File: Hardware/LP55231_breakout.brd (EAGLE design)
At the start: 25.4 x 25.4 mm, 13 parts

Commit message: PCB Work in progress.
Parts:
- removed LED3: LED-TRICOLOR-NO-COMPLCC-6-SMD, SparkFun-LED:PLCC-6-LED
- added FD1, FD2: FIDUCIALUFIDUCIAL, SparkFun-Aesthetics:MICRO-FIDUCIAL
- added J1, J2, J3: (no value), SparkFun-Connectors:1X04_NO_SILK_ALL_ROUND
- added J4: (no value), SparkFun-Connectors:1X09_NO_SILK
- added JP3: I2C-PULLUPS, SparkFun-Passives:PAD-JUMPER-3-NC_BY_PASTE_YES_SILK_FULL_BOX
- added LED4: LED-TRICOLOR-5050NO_IC, SparkFun-LED:LED-TRICOLOR-5050
- added R1, R2: 4.7K, SparkFun-Resistors:0603-RES
- moved C2 11.1 mm to (8.89, 14.6), turned to 270 degrees
- moved LED2 8.98 mm to (19.1, 15.2), turned to 180 degrees
- moved LOGO1 8.03 mm to (17.8, 20.3)
- moved C1 8.03 mm to (14.0, 19.1)
- moved C3 6.75 mm to (10.2, 18.4), turned to 0 degrees
- moved LED1 5.24 mm to (19.1, 25.4), turned to 180 degrees
- moved JP1 5.08 mm to (11.4, 26.7)
- moved LOGO2 5.08 mm to (2.54, 1.27)
- moved JP2 5.08 mm to (10.2, 24.1)
- moved U$1 3.59 mm to (12.7, 15.2)
- moved C4 2.62 mm to (7.62, 17.1), turned to 90 degrees
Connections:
- net N$16 renamed ADDR1
- net N$17 renamed ADDR0
- removed net N$1: LED3.AR, U$1.11
- removed net N$10: C1.1, U$1.22
- removed net N$2: LED3.AG, U$1.15
- removed net N$3: LED3.AB, U$1.14
- removed net N$4: LED2.AB, U$1.16
- removed net N$5: LED2.AR, U$1.12
- removed net N$6: LED2.AG, U$1.17
- removed net N$7: LED1.AR, U$1.13
- removed net N$8: LED1.AG, U$1.19
- removed net N$9: LED1.AB, U$1.18
- new net B1: J1.4, LED1.AB, U$1.18
- new net B2: J2.4, LED2.AB, U$1.16
- new net B3: J3.4, LED4.3, U$1.14
- new net G1: J1.3, LED1.AG, U$1.19
- new net G2: J2.3, LED2.AG, U$1.17
- new net G3: J3.3, LED4.1, U$1.15
- new net N$15: U$1.7
- new net N$18: U$1.10
- new net N$19: U$1.5
- new net N$20: U$1.6
- new net N$21: JP3.1, R2.2
- new net N$22: JP3.3, R1.2
- new net R1: J1.1, LED1.AR, U$1.13
- new net R2: J2.1, LED2.AR, U$1.12
- new net R3: J3.1, LED4.2, U$1.11
- new net SCL: J4.4, R1.1, U$1.9
- new net SDA: J4.3, R2.1, U$1.8
- new net VOUT: C1.1, J4.9, U$1.22
- net GND: now also J1.2, J2.2, J3.2, J4.1, LED4.4, LED4.5, LED4.6; no longer LED3.CB, LED3.CG, LED3.CR
- net VCC: now also J4.2, JP3.2
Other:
- board size 25.4 x 25.4 mm -> 26.7 x 30.5 mm
- board text added: "B1"
- board text added: "B2"
- board text added: "B3"
- board text added: "G1"
- board text added: "G2"
- board text added: "G3"
- board text added: "GND"
- board text added: "R1"
- board text added: "R2"
- board text added: "R3"
- board text added: "SCL"
- board text added: "SDA"
- board text added: "V01"
- board text added: "VCC"
- board text added: "VOUT"

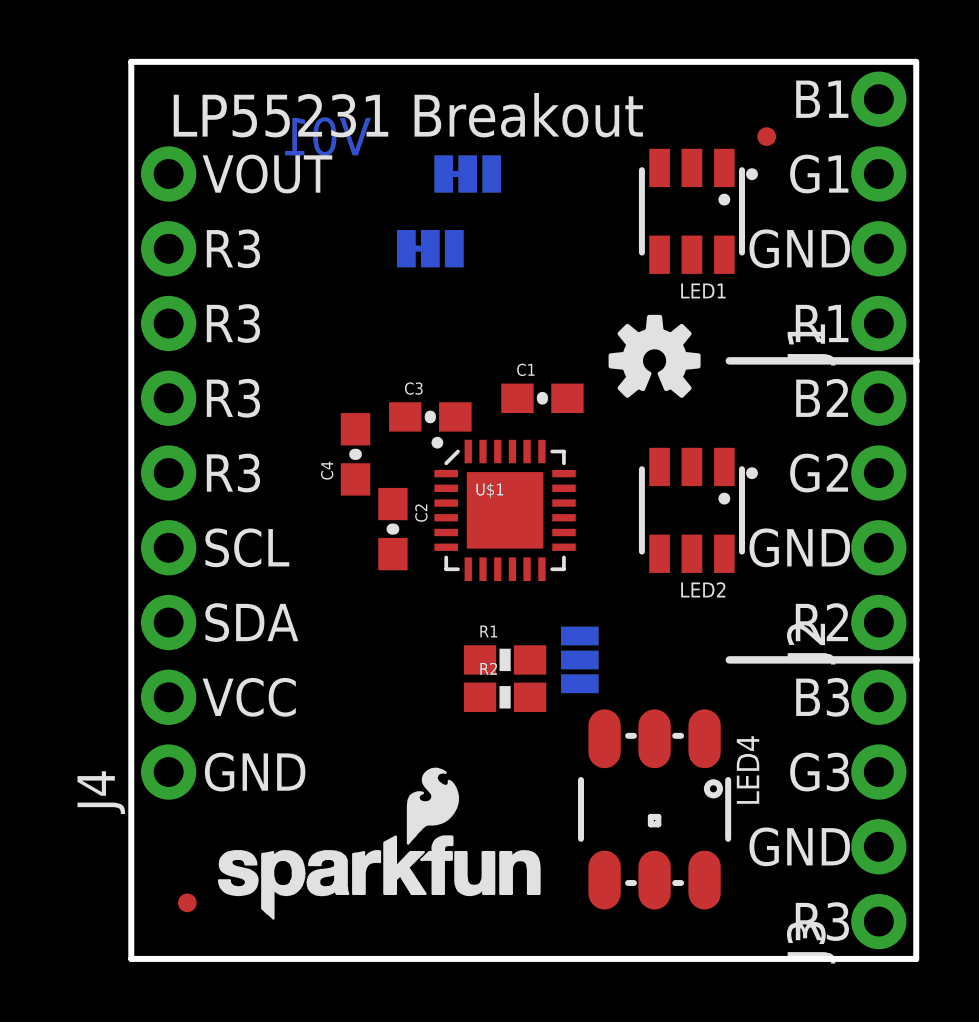
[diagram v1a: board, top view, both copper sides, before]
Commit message: Incremental PCB routing checkin.
Eagle crashed and I'm paranoid now.
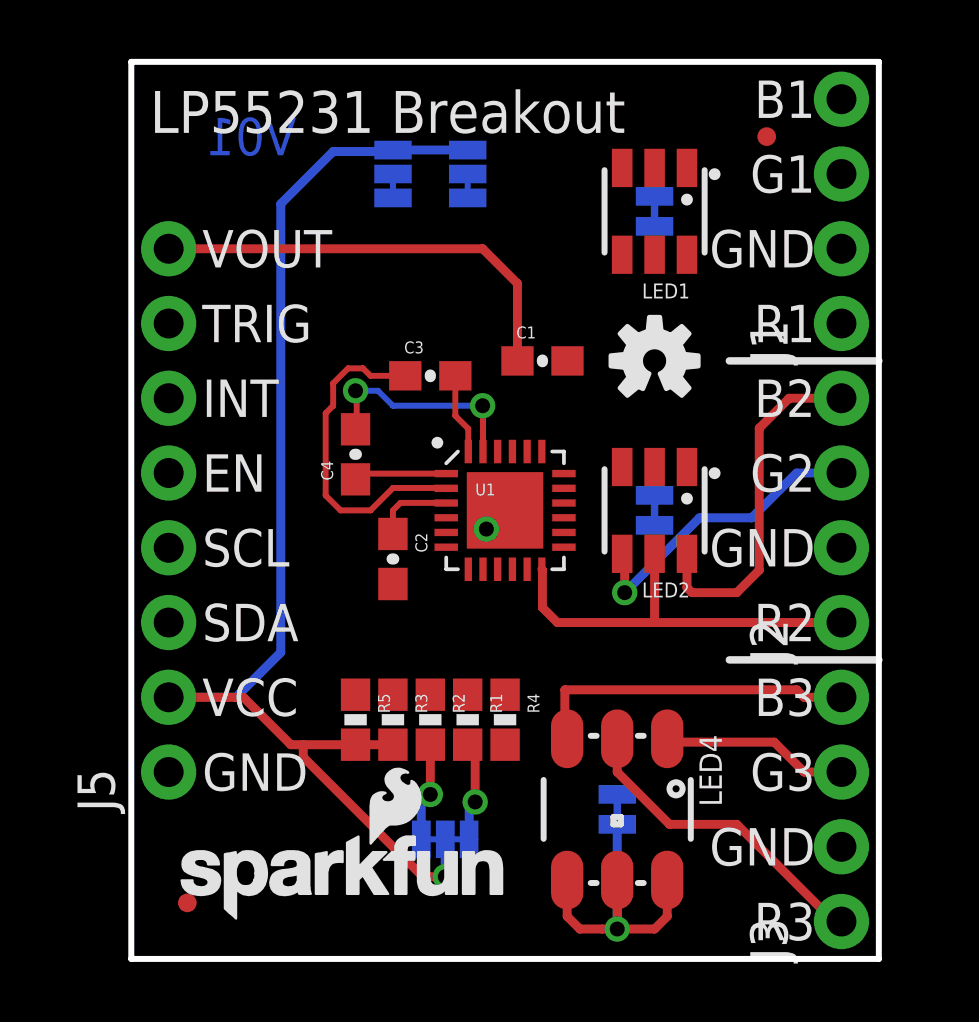
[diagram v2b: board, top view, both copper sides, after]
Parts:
- removed J4: (no value), SparkFun-Connectors:1X09_NO_SILK
- added J5: To micro, SparkFun-Connectors:1X08_NO_SILK
- added JP4: Defeat LED1, SparkFun-Passives:PAD-JUMPER-2-NC_BY_TRACE_YES_SILK
- added JP5: Defeat LED2, SparkFun-Passives:PAD-JUMPER-2-NC_BY_TRACE_YES_SILK
- added JP6: Defeat LED3, SparkFun-Passives:PAD-JUMPER-2-NC_BY_TRACE_YES_SILK
- added R3, R4, R5: 150K, SparkFun-Resistors:0603-RES
- J1, J2, J3: value (none) -> USER LED
- JP3: device SparkFun-Passives:PAD-JUMPER-3-NC_BY_PASTE_YES_SILK_FULL_BOX -> SparkFun-Passives:PAD-JUMPER-3-3OF3_NC_BY_TRACE_YES_SILK_FULL_BOX
- moved JP3 7.62 mm to (10.7, 4.06), turned to 180 degrees
- moved JP2 2.84 mm to (8.89, 26.7), turned to 270 degrees
- moved R2 2.65 mm to (10.2, 8.13), turned to 270 degrees
- moved R1 2.40 mm to (11.4, 8.13), turned to 270 degrees
- moved C3 1.40 mm to (10.2, 19.8)
- moved LOGO2 1.27 mm to (1.27, 1.27)
- moved C1 1.27 mm to (14.0, 20.3)
- moved J1 1.27 mm to (24.1, 21.6)
- moved J2 1.27 mm to (24.1, 11.4)
- moved J3 1.27 mm to (24.1, 1.27)
- moved LED1 1.27 mm to (17.8, 25.4)
- moved LED2 1.27 mm to (17.8, 15.2)
- moved LED4 1.27 mm to (16.5, 5.08)
- moved C2 1.02 mm to (8.89, 13.6)
- turned JP1 to 270 degrees
- renumbered U$1 to U1
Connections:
- removed net N$15: U1.7
- removed net N$18: U1.10
- removed net N$19: U1.5
- removed net N$20: U1.6
- new net EN: J5.5, R5.1, U1.5
- new net INT: J5.6, R3.1, U1.7
- new net N$1: JP6.2, LED4.4, LED4.5, LED4.6
- new net N$2: JP5.2, LED2.CB, LED2.CG, LED2.CR
- new net N$3: JP4.2, LED1.CB, LED1.CG, LED1.CR
- new net TRIG: J5.7, R4.1, U1.10
- net GND: now also J5.1, JP4.1, JP5.1, JP6.1, R4.2, U1.6; no longer J4.1, LED1.CB, LED1.CG, LED1.CR, LED2.CB, LED2.CG, LED2.CR, LED4.4, LED4.5, LED4.6
- net SCL: now also J5.4; no longer J4.4
- net SDA: now also J5.3; no longer J4.3
- net VCC: now also J5.2, R3.2, R5.2; no longer J4.2
- net VOUT: now also J5.8; no longer J4.9
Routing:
- net VCC: track 0.00 -> 46.1 mm, vias 0 -> 1
- net VOUT: track 0.00 -> 15.0 mm
- net R2: track 0.00 -> 14.0 mm
- net B2: track 0.00 -> 12.0 mm
- net N$1: track 0.00 -> 11.4 mm, vias 0 -> 1
- net N$11: track 0.00 -> 11.3 mm
- net B3: track 0.00 -> 11.2 mm
- net R3: track 0.00 -> 10.9 mm
- net G2: track 0.00 -> 10.4 mm, vias 0 -> 1
- net N$14: track 0.00 -> 7.43 mm, vias 0 -> 2
- net G3: track 0.00 -> 6.26 mm
- net N$22: track 0.00 -> 3.40 mm, vias 0 -> 1
- net N$21: track 0.00 -> 3.34 mm, vias 0 -> 1
- net N$13: track 0.00 -> 3.16 mm
- net N$12: track 0.00 -> 2.75 mm
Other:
- board size 26.7 x 30.5 mm -> 25.4 x 30.5 mm
- board text added: "EN"
- board text added: "INT"
- board text added: "TRIG"

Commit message: Routing approaching completion.
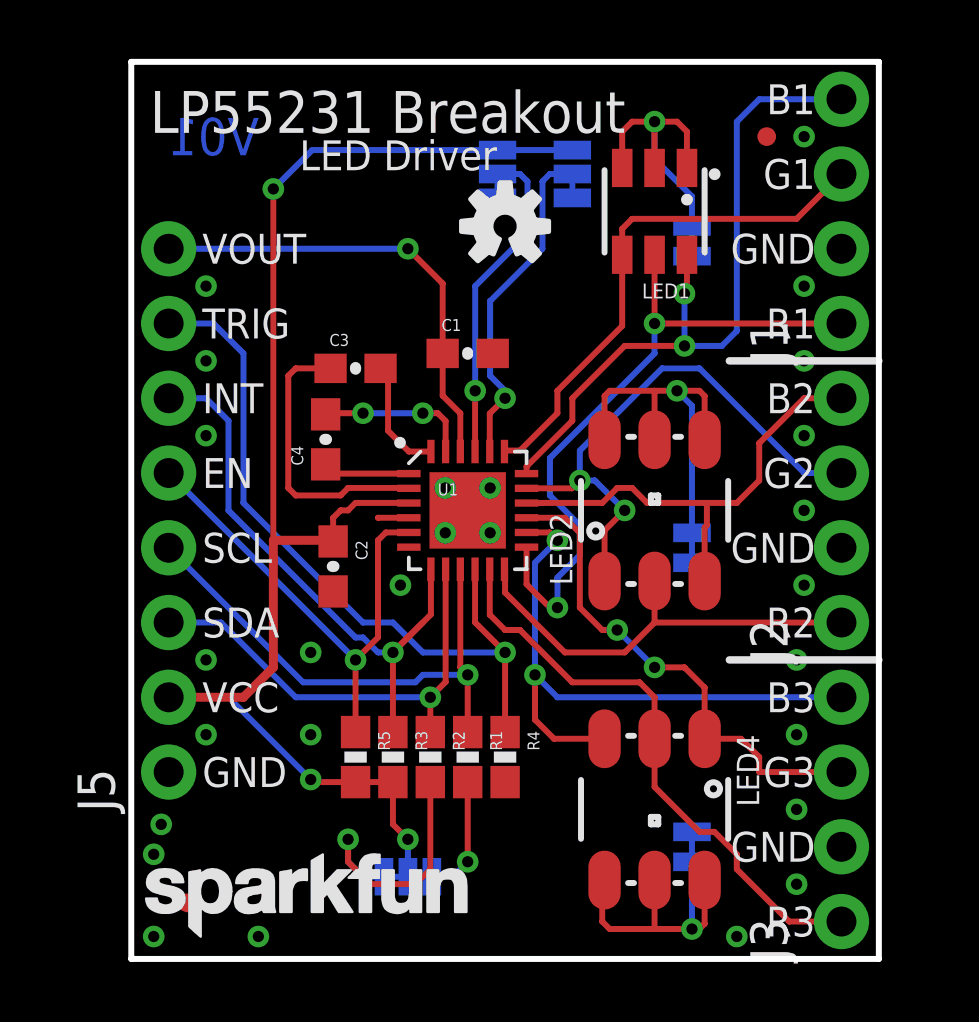
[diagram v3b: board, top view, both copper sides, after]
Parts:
- added LOGO3: SFE_LOGO_FLAME.1_INCH, SparkFun-Aesthetics:SFE_LOGO_FLAME_.1
- JP4, JP5, JP6: device SparkFun-Passives:PAD-JUMPER-2-NC_BY_TRACE_YES_SILK -> SparkFun-Passives:PAD-JUMPER-2-NC_BY_TRACE_NO_SILK
- LED2: value LED-TRICOLOR-NO-COMPLCC-6-SMD -> LED-TRICOLOR-5050NO_IC; device SparkFun-LED:PLCC-6-LED -> SparkFun-LED:LED-TRICOLOR-5050
- LOGO2: value SFE_LOGO_NAME_FLAME.1_INCH -> SFE_LOGO_NAME.1_INCH; device SparkFun-Aesthetics:SFE_LOGO_NAME_FLAME_.1 -> SparkFun-Aesthetics:SFE_LOGO_NAME_.1
- moved LOGO1 6.83 mm to (12.7, 24.9)
- moved JP1 3.56 mm to (15.0, 26.7)
- moved JP2 3.56 mm to (12.4, 26.7)
- moved JP6 2.84 mm to (19.1, 3.81)
- moved C1 2.55 mm to (11.4, 20.6)
- moved C3 2.55 mm to (7.62, 20.1)
- moved C2 2.05 mm to (6.86, 13.3)
- moved JP3 1.80 mm to (9.40, 2.79)
- moved JP5 1.80 mm to (19.1, 14.0)
- moved LOGO2 1.63 mm to (0.00, 0.25)
- moved JP4 1.63 mm to (19.1, 24.4)
- moved R1 1.27 mm to (11.4, 6.86)
- moved R2 1.27 mm to (10.2, 6.86)
- moved R3 1.27 mm to (8.89, 6.86)
- moved R4 1.27 mm to (12.7, 6.86)
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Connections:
- net B2: now also LED2.3; no longer LED2.AB
- net G2: now also LED2.1; no longer LED2.AG
- net N$2: now also LED2.4, LED2.5, LED2.6; no longer LED2.CB, LED2.CG, LED2.CR
- net R2: now also LED2.2; no longer LED2.AR
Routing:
- net TRIG: track 0.00 -> 25.0 mm, vias 0 -> 1
- net B1: track 0.00 -> 23.9 mm, vias 0 -> 2
- net R1: track 0.00 -> 23.2 mm, vias 0 -> 2
- net INT: track 0.00 -> 20.5 mm, vias 0 -> 1
- net SCL: track 0.00 -> 17.8 mm, vias 0 -> 1
- net G1: track 0.00 -> 17.7 mm
- net EN: track 0.00 -> 17.0 mm, vias 0 -> 1
- net SDA: track 0.00 -> 15.7 mm, vias 0 -> 1
- net N$2: track 0.00 -> 13.2 mm, vias 0 -> 1
- net ADDR0: track 0.00 -> 11.5 mm, vias 0 -> 1
- net ADDR1: track 0.00 -> 11.0 mm, vias 0 -> 1
- net G3: track 6.26 -> 17.1 mm, vias 0 -> 2
- net N$3: track 0.00 -> 10.6 mm, vias 0 -> 1
- net B3: track 11.2 -> 21.3 mm, vias 0 -> 2
- net R3: track 10.9 -> 19.9 mm
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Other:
- board text added: "0x32"
- board text added: "0x33"
- board text added: "0x34"
- board text added: "0x35"
- board text added: "A0"
- board text added: "A1"
- board text added: "All Dimensions In Inches"
- board text added: "D1"
- board text added: "D1,2,3 Defeat onboard LEDs"
- board text added: "D3"
- board text added: "I2C Pullups"
- board text added: "LED Driver"

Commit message: Prepping for review.
BOM created, checklist scrubbed.
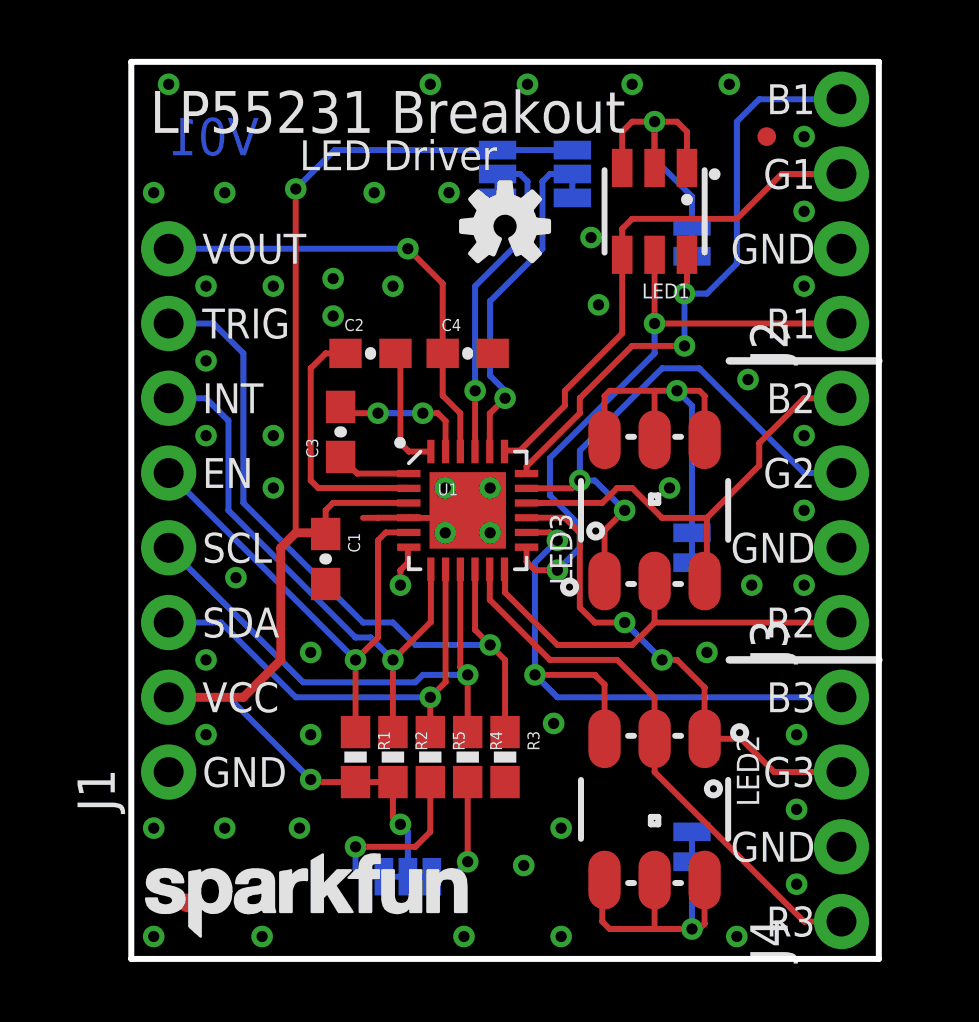
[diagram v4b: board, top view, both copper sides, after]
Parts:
- removed J5: To micro, SparkFun-Connectors:1X08_NO_SILK
- removed LED4: LED-TRICOLOR-5050NO_IC, SparkFun-LED:LED-TRICOLOR-5050
- added J4: USER LED, SparkFun-Connectors:1X04_NO_SILK_ALL_ROUND
- added LED3: TRICOLOR-5050, SparkFun-LED:LED-TRICOLOR-5050
- C2: value 1.0uF -> 0.47uf
- C4: value 0.47uf -> 1.0uF
- J1: value USER LED -> To micro; device SparkFun-Connectors:1X04_NO_SILK_ALL_ROUND -> SparkFun-Connectors:1X08_NO_SILK
- JP1: value A0 -> A1
- JP2: value A1 -> I2C-PULLUPS; device SparkFun-Passives:PAD-JUMPER-3-2OF3_NC_BY_TRACE_YES_SILK_FULL_BOX -> SparkFun-Passives:PAD-JUMPER-3-3OF3_NC_BY_TRACE_YES_SILK_FULL_BOX
- JP3: value I2C-PULLUPS -> A0; device SparkFun-Passives:PAD-JUMPER-3-3OF3_NC_BY_TRACE_YES_SILK_FULL_BOX -> SparkFun-Passives:PAD-JUMPER-3-2OF3_NC_BY_TRACE_YES_SILK_FULL_BOX
- LED1: value LED-TRICOLOR-NO-COMPLCC-6-SMD -> TRICOLOR-PLCC-6
- LED2: value LED-TRICOLOR-5050NO_IC -> TRICOLOR-5050
- LOGO1: value OSHW-LOGOS -> SFE_LOGO_FLAME.1_INCH; device SparkFun-Aesthetics:OSHW-LOGO-S -> SparkFun-Aesthetics:SFE_LOGO_FLAME_.1
- LOGO3: value SFE_LOGO_FLAME.1_INCH -> OSHW-LOGOS; device SparkFun-Aesthetics:SFE_LOGO_FLAME_.1 -> SparkFun-Aesthetics:OSHW-LOGO-S
- R1, R2: value 4.7K -> 150K
- R4, R5: value 150K -> 4.7K
- moved FD1 32.6 mm to (21.6, 27.9)
- moved FD2 32.6 mm to (1.91, 1.91)
- moved J1 27.5 mm to (1.27, 6.35)
- moved JP3 24.5 mm to (15.0, 26.7), turned to 270 degrees
- moved JP2 24.1 mm to (9.40, 2.79), turned to 180 degrees
- moved LOGO1 13.2 mm to (12.7, 11.7), flipped to the bottom
- moved J2 10.2 mm to (24.1, 21.6)
- moved J3 10.2 mm to (24.1, 11.4)
- moved LED2 10.2 mm to (17.8, 5.08), turned to 270 degrees
- moved C1 8.49 mm to (6.60, 13.6), turned to 270 degrees
- moved C2 7.35 mm to (8.13, 20.6), turned to 0 degrees
- moved C4 5.64 mm to (11.4, 20.6), turned to 0 degrees
- moved LOGO3 5.08 mm to (12.7, 24.9), flipped to the top
- moved R1 3.81 mm to (7.62, 6.86)
- moved R3 3.81 mm to (12.7, 6.86)
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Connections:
- net ADDR0: now also JP3.2; no longer JP1.2
- net ADDR1: now also JP1.2; no longer JP2.2
- net B1: now also J2.4; no longer J1.4
- net B2: now also J3.4, LED3.3; no longer J2.4, LED2.3
- net B3: now also J4.4, LED2.3; no longer J3.4, LED4.3
- net EN: now also J1.5, R1.1; no longer J5.5, R5.1
- net G1: now also J2.3; no longer J1.3
- net G2: now also J3.3, LED3.1; no longer J2.3, LED2.1
- net G3: now also J4.3, LED2.1; no longer J3.3, LED4.1
- net GND: now also C4.2, J1.1, J4.2, JP3.3, R3.2; no longer C2.2, J1.2, J5.1, JP2.3, R4.2
- net INT: now also J1.6, R2.1; no longer J5.6, R3.1
- net N$1: now also LED2.4, LED2.5, LED2.6; no longer LED4.4, LED4.5, LED4.6
- net N$11: now also C2.1; no longer C3.1
- net N$12: now also C2.2; no longer C3.2
- net N$13: now also C3.1; no longer C4.1
- net N$14: now also C3.2; no longer C4.2
- net N$2: now also LED3.4, LED3.5, LED3.6; no longer LED2.4, LED2.5, LED2.6
- net N$21: now also JP2.1, R5.2; no longer JP3.1, R2.2
- net N$22: now also JP2.3, R4.2; no longer JP3.3, R1.2
- net R1: now also J2.1; no longer J1.1
- net R2: now also J3.1, LED3.2; no longer J2.1, LED2.2
- net R3: now also J4.1, LED2.2; no longer J3.1, LED4.2
- net SCL: now also J1.4, R4.1; no longer J5.4, R1.1
- net SDA: now also J1.3, R5.1; no longer J5.3, R2.1
- net TRIG: now also J1.7, R3.1; no longer J5.7, R4.1
- net VCC: now also C1.1, J1.2, JP2.2, JP3.1, R1.2, R2.2; no longer C2.1, J5.2, JP2.1, JP3.2, R3.2, R5.2
- net VOUT: now also C4.1, J1.8; no longer C1.1, J5.8
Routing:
- net GND: track 2.13 -> 8.04 mm, vias 27 -> 54
- net N$21: track 9.23 -> 6.27 mm
- net R1: track 23.2 -> 20.9 mm
- net B1: track 23.9 -> 21.6 mm
- net INT: track 20.5 -> 19.2 mm
- net VCC: track 48.8 -> 47.5 mm
- net N$11: track 9.66 -> 8.65 mm
- net R3: track 19.9 -> 19.0 mm
- net TRIG: track 25.0 -> 24.4 mm
- net N$12: track 4.07 -> 4.63 mm

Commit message: Straight out of QFN.
Fewer bends & kinks.
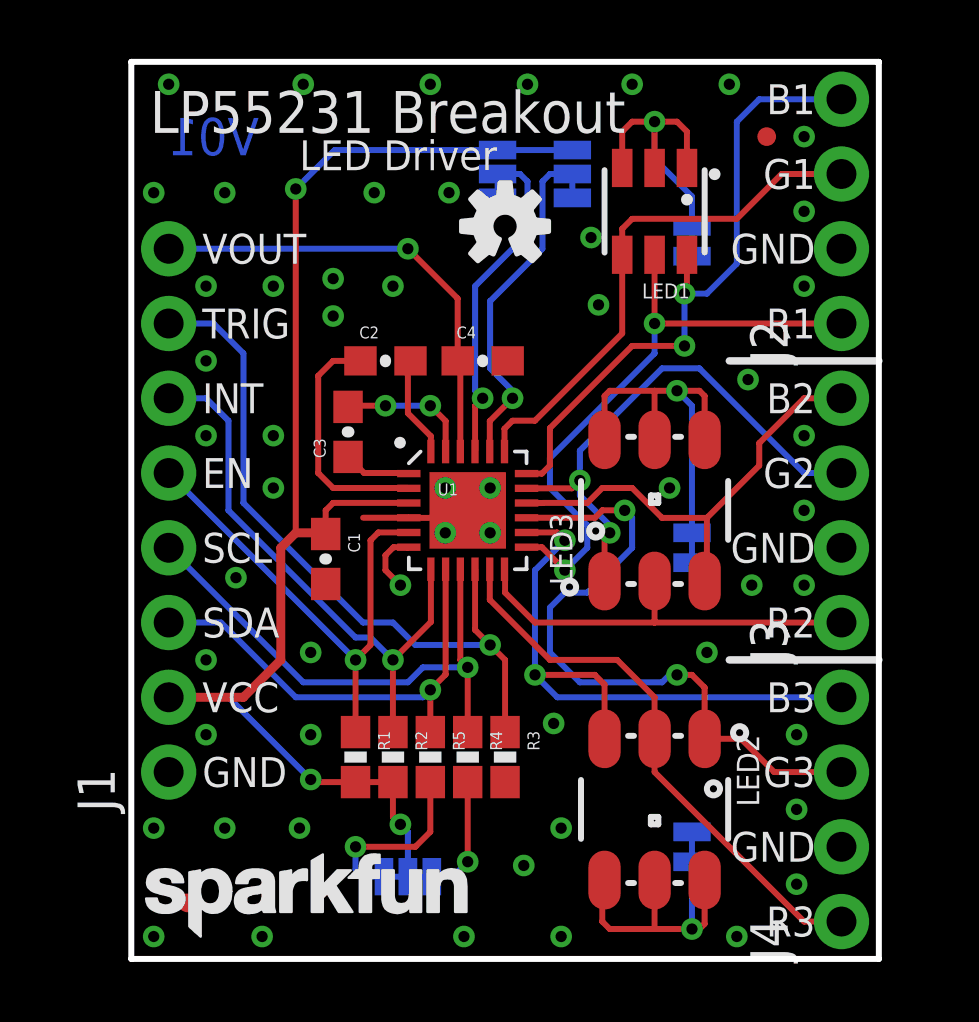
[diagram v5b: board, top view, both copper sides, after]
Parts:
- moved C4 0.57 mm to (11.9, 20.3)
- moved C2 0.57 mm to (8.64, 20.3)
- moved C3 0.25 mm to (7.37, 17.9)
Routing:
- net G3: track 16.8 -> 22.8 mm
- net N$12: track 4.63 -> 3.69 mm
- net G2: track 19.1 -> 18.4 mm
- net R2: track 14.7 -> 14.1 mm
- net GND: track 8.04 -> 8.55 mm, vias 54 -> 55
